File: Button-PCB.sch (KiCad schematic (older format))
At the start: 31 parts, among them J1 VPP, J10 Strip 4, J11 3V3, J2 UART, J3 Strip 1, J4 Strip 3, J5 RES, J7 Button, J8 Power IN, J9 Strip 2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

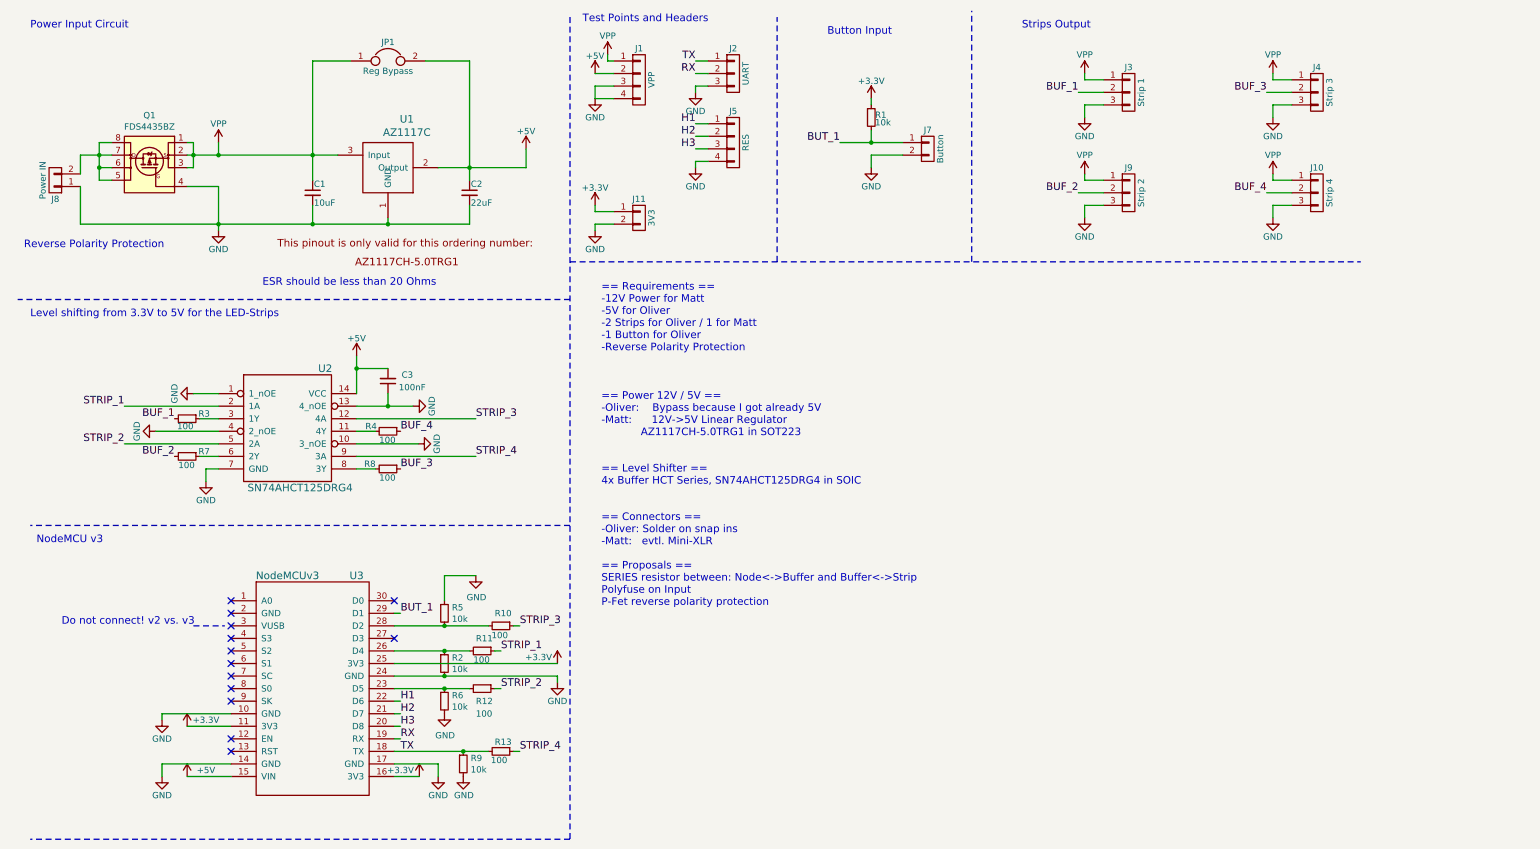
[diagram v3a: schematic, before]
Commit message: Rename nets so that strip 3 drives buf 3 instead of buf 4.
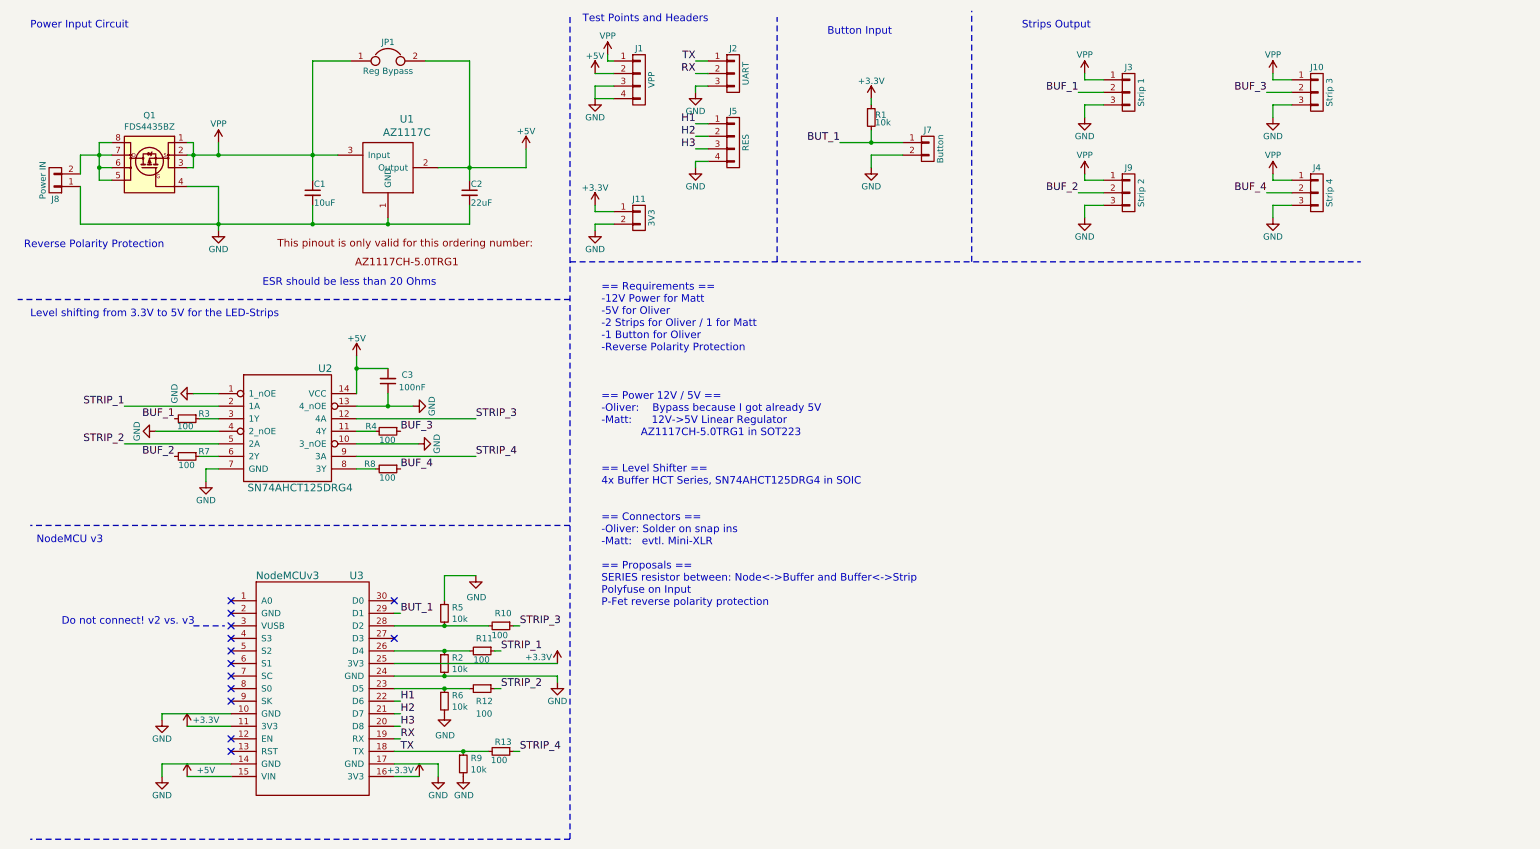
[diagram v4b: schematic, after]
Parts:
- J10: value Strip 4 -> Strip 3
- J4: value Strip 3 -> Strip 4
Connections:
- net BUF_3: now also J10.2 (P2), R4.1; no longer J4.2 (P2), R8.1
- net BUF_4: now also J4.2 (P2), R8.1; no longer J10.2 (P2), R4.1
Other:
- moved on the sheet: J10, J4
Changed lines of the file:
@@
 L CONN_01X03 J10
 U 1 1 593F28A9
+P 10850 1150
+F 0 "J10" H 10850 1350 50  0000 C CNN
+F 1 "Strip 3" V 10950 1150 50  0000 C CNN
+F 2 "Pin_Headers:Pin_Header_Angled_1x03_Pitch2.54mm" H 10850 1150 50  0001 C CNN
+F 3 "" H 10850 1150 50  0001 C CNN
+	1    10850 1150
+	1    0    0    -1
+$EndComp
+$Comp
+L CONN_01X03 J4
+U 1 1 593F28AF
 P 10850 1950
-F 0 "J10" H 10850 2150 50  0000 C CNN
+F 0 "J4" H 10850 2150 50  0000 C CNN
 F 1 "Strip 4" V 10950 1950 50  0000 C CNN
 F 2 "Pin_Headers:Pin_Header_Angled_1x03_Pitch2.54mm" H 10850 1950 50  0001 C CNN
 F 3 "" H 10850 1950 50  0001 C CNN
 	1    10850 1950
-	1    0    0    -1
-$EndComp
-$Comp
-L CONN_01X03 J4
-U 1 1 593F28AF
-P 10850 1150
-F 0 "J4" H 10850 1350 50  0000 C CNN
-F 1 "Strip 3" V 10950 1150 50  0000 C CNN
-F 2 "Pin_Headers:Pin_Header_Angled_1x03_Pitch2.54mm" H 10850 1150 50  0001 C CNN
-F 3 "" H 10850 1150 50  0001 C CNN
-	1    10850 1150
 	1    0    0    -1
 $EndComp
@@
 L GND #PWR013
 U 1 1 593F28C1
+P 10500 2150
+F 0 "#PWR013" H 10500 1900 50  0001 C CNN
+F 1 "GND" H 10500 2000 50  0000 C CNN
+F 2 "" H 10500 2150 50  0001 C CNN
+F 3 "" H 10500 2150 50  0001 C CNN
+	1    10500 2150
+	1    0    0    -1
+$EndComp
+$Comp
+L GND #PWR014
+U 1 1 593F28C7
 P 10500 1350
-F 0 "#PWR013" H 10500 1100 50  0001 C CNN
+F 0 "#PWR014" H 10500 1100 50  0001 C CNN
 F 1 "GND" H 10500 1200 50  0000 C CNN
 F 2 "" H 10500 1350 50  0001 C CNN
 F 3 "" H 10500 1350 50  0001 C CNN
 	1    10500 1350
-	1    0    0    -1
-$EndComp
-$Comp
-L GND #PWR014
-U 1 1 593F28C7
-P 10500 2150
-F 0 "#PWR014" H 10500 1900 50  0001 C CNN
-F 1 "GND" H 10500 2000 50  0000 C CNN
-F 2 "" H 10500 2150 50  0001 C CNN
-F 3 "" H 10500 2150 50  0001 C CNN
-	1    10500 2150
 	1    0    0    -1
 $EndComp
@@
 L VPP #PWR016
 U 1 1 593F50FF
+P 10500 1800
+F 0 "#PWR016" H 10500 1650 50  0001 C CNN
+F 1 "VPP" H 10500 1950 50  0000 C CNN
+F 2 "" H 10500 1800 50  0001 C CNN
+F 3 "" H 10500 1800 50  0001 C CNN
+	1    10500 1800
+	1    0    0    -1
+$EndComp
+$Comp
+L VPP #PWR017
+U 1 1 593F513D
 P 10500 1000
-F 0 "#PWR016" H 10500 850 50  0001 C CNN
+F 0 "#PWR017" H 10500 850 50  0001 C CNN
 F 1 "VPP" H 10500 1150 50  0000 C CNN
 F 2 "" H 10500 1000 50  0001 C CNN
 F 3 "" H 10500 1000 50  0001 C CNN
 	1    10500 1000
-	1    0    0    -1
-$EndComp
-$Comp
-L VPP #PWR017
-U 1 1 593F513D
-P 10500 1800
-F 0 "#PWR017" H 10500 1650 50  0001 C CNN
-F 1 "VPP" H 10500 1950 50  0000 C CNN
-F 2 "" H 10500 1800 50  0001 C CNN
-F 3 "" H 10500 1800 50  0001 C CNN
-	1    10500 1800
 	1    0    0    -1
 $EndComp
@@
 Text Label 1750 4050 2    60   ~ 0
 BUF_2
+Text Label 3550 3850 0    60   ~ 0
+BUF_3
 Text Label 3550 4150 0    60   ~ 0
-BUF_3
-Text Label 3550 3850 0    60   ~ 0
 BUF_4
 $Comp
@@
 	1850 6600 2200 6600
 Wire Wire Line
-	10500 2150 10500 2050
-Wire Wire Line
-	10500 2050 10650 2050
+	10500 1350 10500 1250
+Wire Wire Line
+	10500 1250 10650 1250
+Wire Wire Line
+	10650 1150 10450 1150
+Wire Wire Line
+	10650 2050 10500 2050
+Wire Wire Line
+	10500 2050 10500 2150
 Wire Wire Line
 	10650 1950 10450 1950
 Wire Wire Line
-	10650 1250 10500 1250
-Wire Wire Line
-	10500 1250 10500 1350
-Wire Wire Line
-	10650 1150 10450 1150
-Wire Wire Line
 	9000 1000 9000 1050
 Wire Wire Line
@@
 	9000 1850 9150 1850
 Wire Wire Line
+	10500 1000 10500 1050
+Wire Wire Line
+	10500 1050 10650 1050
+Wire Wire Line
 	10500 1800 10500 1850
 Wire Wire Line
 	10500 1850 10650 1850
-Wire Wire Line
-	10500 1000 10500 1050
-Wire Wire Line
-	10500 1050 10650 1050
 Wire Notes Line
 	4900 2500 11200 2500

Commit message: hacking bugs
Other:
- note added: "Something with the TX pin doesn't work, booting is not working..."
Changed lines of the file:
@@
 LIBS:nodemcuv3
 LIBS:Button-PCB-cache
-EELAYER 26 0
+EELAYER 25 0
 EELAYER END
 $Descr A4 11693 8268
@@
 	1    0    0    -1
 $EndComp
+Text Notes 5150 6150 0    118  ~ 0
+Something with the TX pin doesn't work, booting is not working...
 $EndSCHEMATC
